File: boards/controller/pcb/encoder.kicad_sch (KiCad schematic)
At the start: 10 parts, among them SW3 EC11E15204A3

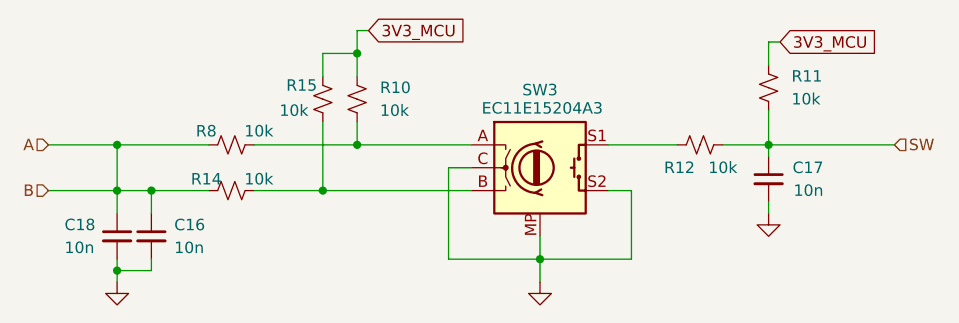
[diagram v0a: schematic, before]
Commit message: controller: Update PCB
Signed-off-by: Nicholas Loehrke <nicholasnloehrke@gmail.com>
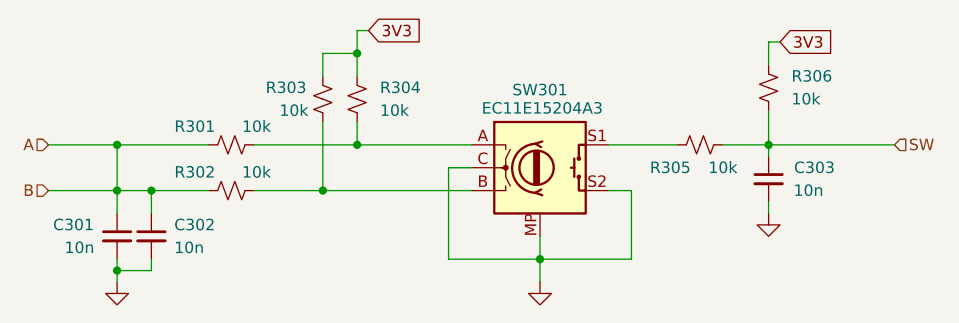
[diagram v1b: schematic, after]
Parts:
- renumbered C18 to C301, C16 to C302, C17 to C303, R8 to R301, R14 to R302, R15 to R303, R10 to R304, R12 to R305, R11 to R306, SW3 to SW301
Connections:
- net 3V3_MCU renamed 3V3
